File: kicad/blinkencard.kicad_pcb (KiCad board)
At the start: 2 copper layers, 89 x 51 mm, 68 parts, among them Q1 BC847, Q2 BC847, Q3 BC847, Q4 BC847, Q5 BC847, SW1 LEFT, SW2 1, SW3 0, SW4 RIGHT, U1 ICE40UP5K-SG48ITR, U2 ESP32-WROOM-32D

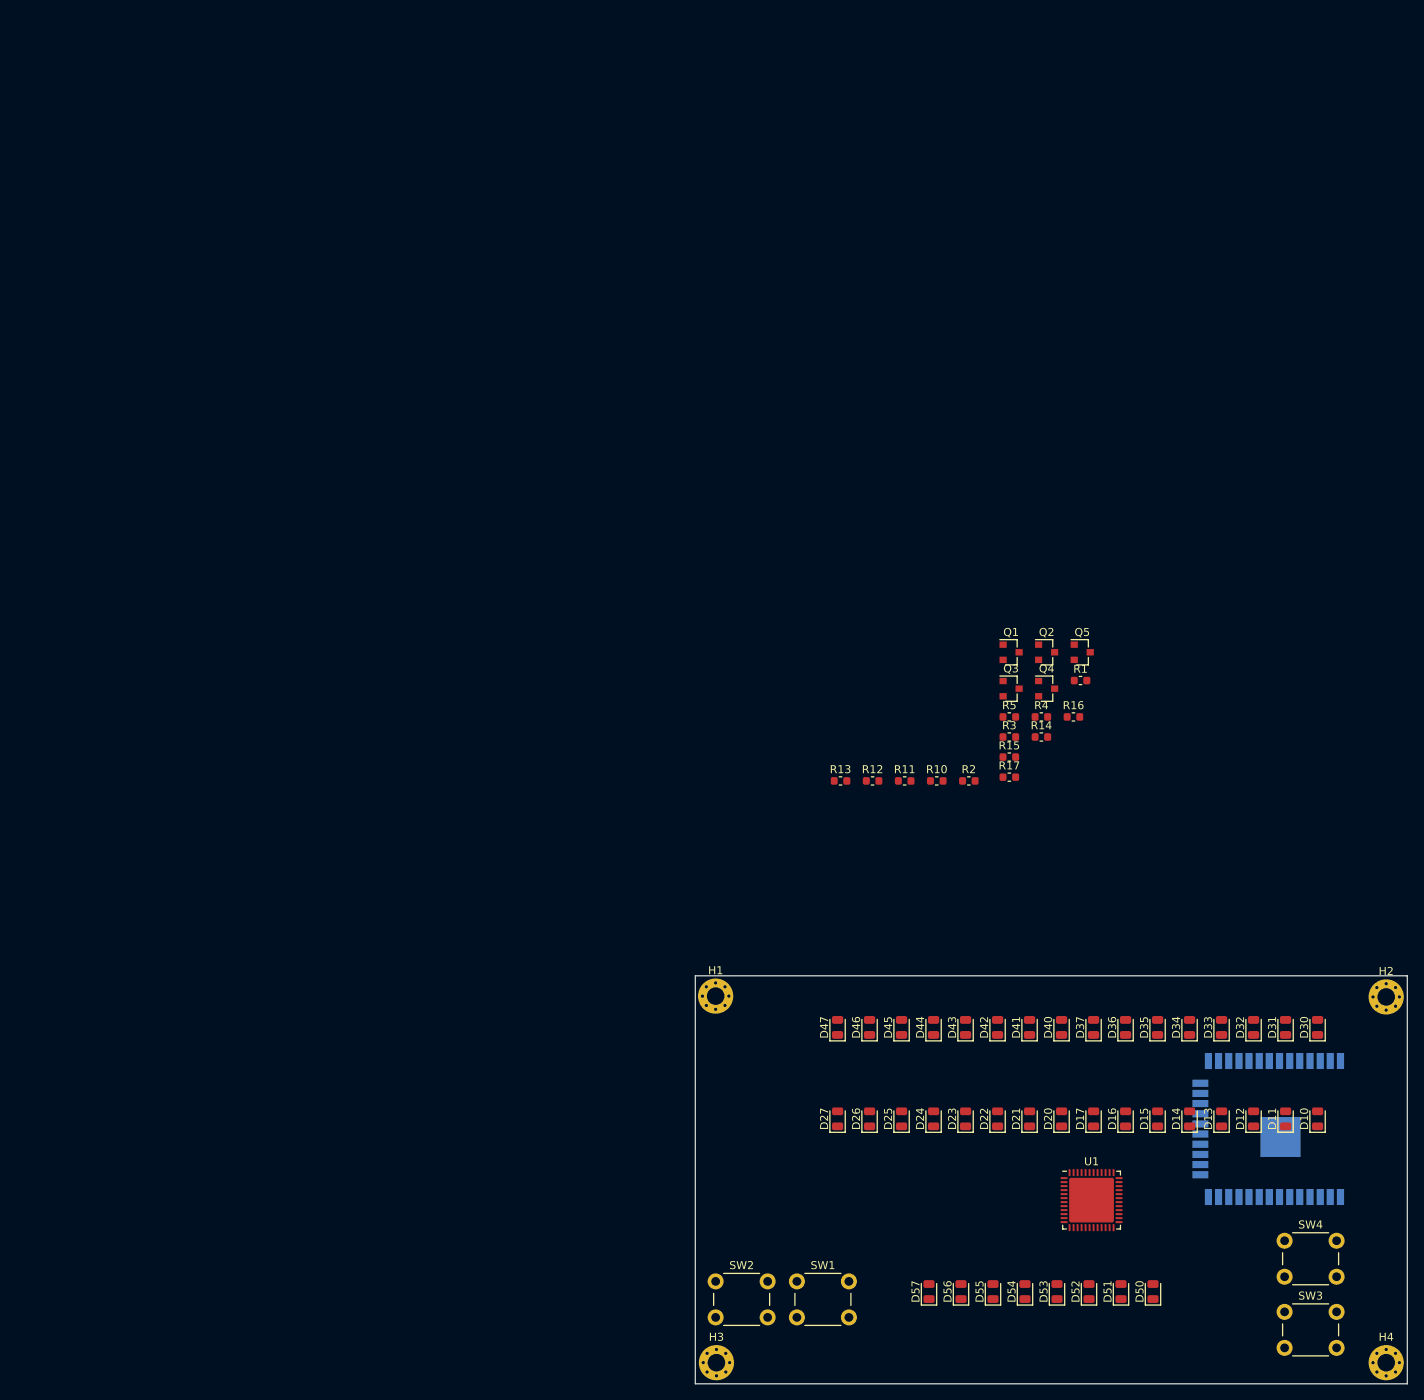
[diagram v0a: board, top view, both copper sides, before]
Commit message: LED layout in progress
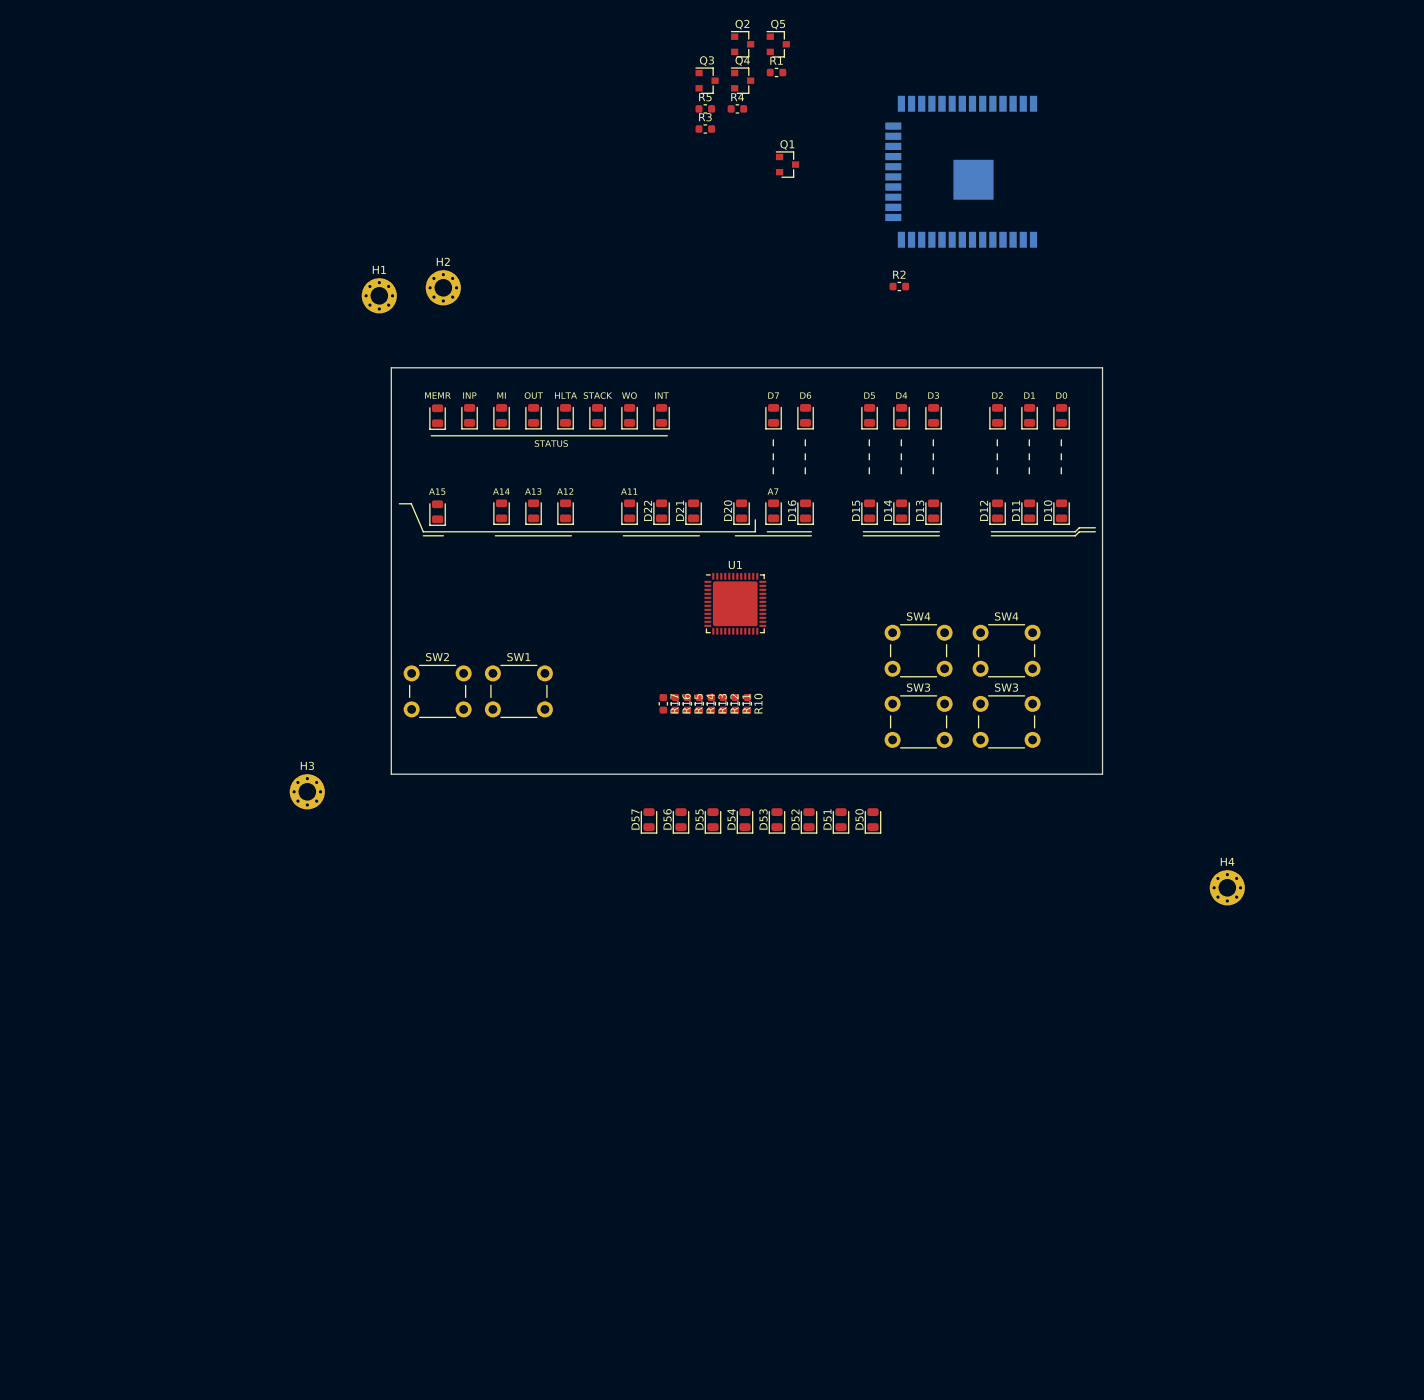
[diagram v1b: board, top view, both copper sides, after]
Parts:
- added SW3: 0, Button_Switch_THT:SW_PUSH_6mm_H5mm, F.Cu at (62.7, 42.0)
- added SW4: RIGHT, Button_Switch_THT:SW_PUSH_6mm_H5mm, F.Cu at (62.7, 33.1)
- moved H2 147.5 mm to (6.50, -10.0)
- moved U2 125.7 mm to (72.0, -24.5)
- moved H1 97.1 mm to (-1.50, -9.00)
- moved D40 91.4 mm to (33.8, 5.95)
- moved D41 91.4 mm to (29.8, 5.95)
- moved D42 91.4 mm to (25.8, 5.95)
- moved D43 91.4 mm to (21.8, 5.95)
- moved D44 91.4 mm to (17.8, 5.95)
- moved D45 91.4 mm to (13.8, 5.95)
- moved D46 91.4 mm to (9.78, 5.95)
- moved D47 91.3 mm to (5.78, 6.00)
- moved D27 90.9 mm to (5.78, 18.0)
- moved D24 88.8 mm to (21.8, 17.9)
- moved D25 88.8 mm to (17.8, 17.9)
- moved D26 88.8 mm to (13.8, 17.9)
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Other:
- board size 89 x 51 mm -> 88.9 x 50.8 mm
- board text added: "STATUS"

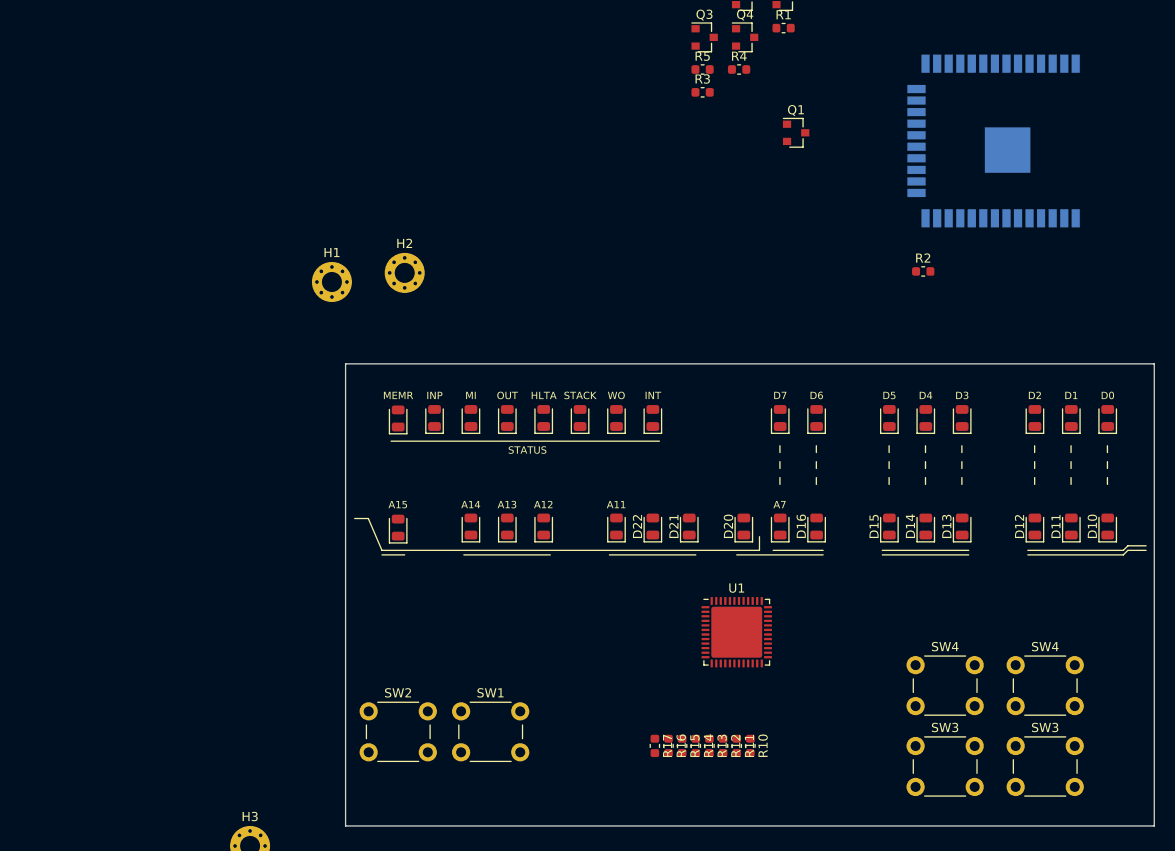
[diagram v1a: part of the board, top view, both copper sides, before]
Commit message: More LED routing
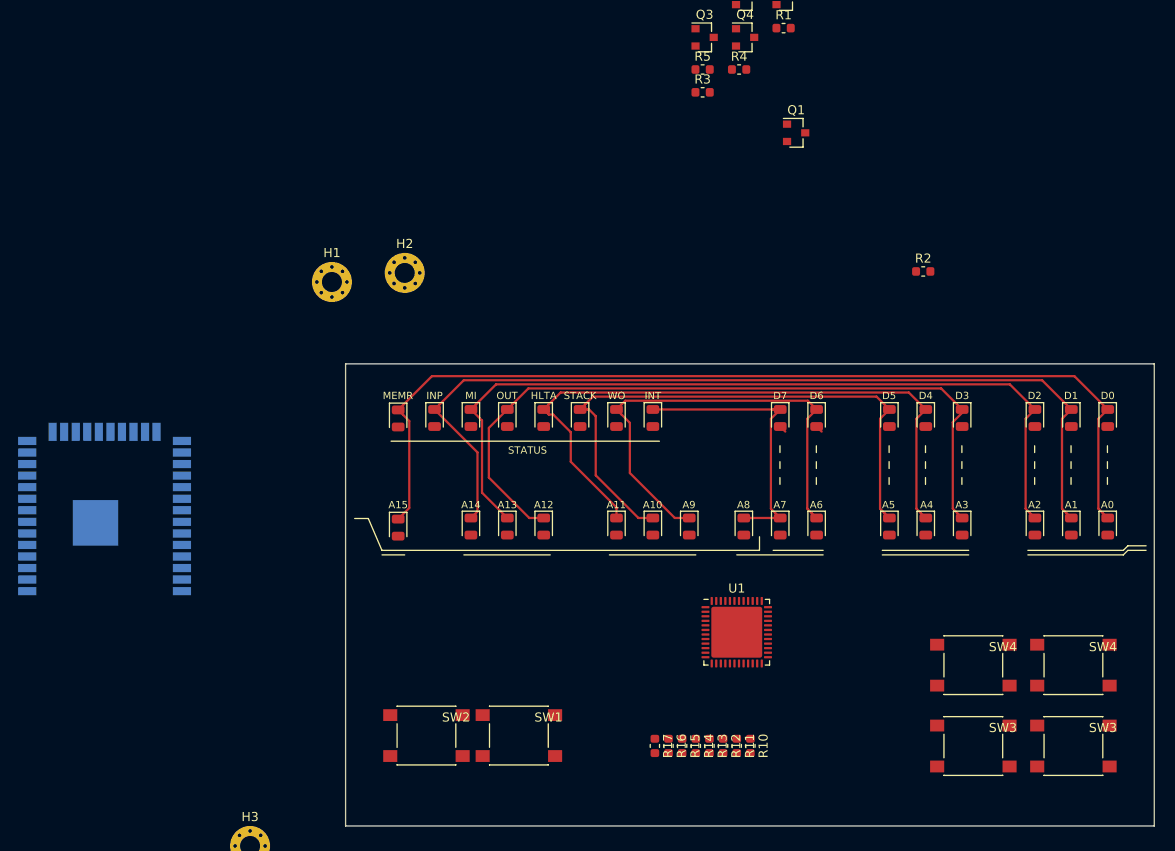
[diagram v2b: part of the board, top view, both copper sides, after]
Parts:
- removed the D12 at (75.8, 17.9)
- added D15: LED_Small, LED_SMD:LED_0805_2012Metric, F.Cu at (75.8, 17.9)
- SW1, SW2, SW3 (x2), SW4 (x2): footprint Button_Switch_THT:SW_PUSH_6mm_H5mm -> Button_Switch_SMD:SW_SPST_PTS645
- moved U2 106.8 mm to (-26.5, 16.7), turned to 0 degrees
- moved SW1 6.88 mm to (19.1, 40.9)
- moved SW2 6.88 mm to (8.89, 40.9)
- moved SW3 6.35 mm to (69.0, 42.0)
- moved SW3 6.35 mm to (80.0, 42.0)
- moved SW4 6.35 mm to (69.0, 33.1)
- moved SW4 6.35 mm to (80.0, 33.1)
- turned D10 to 270 degrees
- turned D11 to 270 degrees
- turned D12 to 270 degrees
- turned D13 to 270 degrees
- turned D14 to 270 degrees
- turned D16 to 270 degrees
- turned D17 to 270 degrees
- turned D20 to 270 degrees
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- renumbered D17 to D10, D16 to D11, D15 to D12, D14 to D13, D13 to D14, D11 to D16, D10 to D17, D37 to D30, D36 to D31, D35 to D32, D34 to D33, D33 to D34, D32 to D35, D31 to D36, D30 to D37
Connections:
- D10 pad 1: Net-(D17-Pad1) -> Net-(D10-Pad1)
- D11 pad 1: Net-(D16-Pad1) -> Net-(D11-Pad1)
- D12 pad 1: Net-(D15-Pad1) -> Net-(D12-Pad1)
- D13 pad 1: Net-(D14-Pad1) -> Net-(D13-Pad1)
- D14 pad 1: Net-(D13-Pad1) -> Net-(D14-Pad1)
- D16 pad 1: Net-(D11-Pad1) -> Net-(D16-Pad1)
- D17 pad 1: Net-(D10-Pad1) -> Net-(D17-Pad1)
- D30 pad 1: Net-(D17-Pad1) -> Net-(D10-Pad1)
- D31 pad 1: Net-(D16-Pad1) -> Net-(D11-Pad1)
- D32 pad 1: Net-(D15-Pad1) -> Net-(D12-Pad1)
- D33 pad 1: Net-(D14-Pad1) -> Net-(D13-Pad1)
- D34 pad 1: Net-(D13-Pad1) -> Net-(D14-Pad1)
- D35 pad 1: Net-(D12-Pad1) -> Net-(D15-Pad1)
- D36 pad 1: Net-(D11-Pad1) -> Net-(D16-Pad1)
- D37 pad 1: Net-(D10-Pad1) -> Net-(D17-Pad1)
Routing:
- net Net-(D17-Pad1): track 0.00 -> 106.8 mm
- net Net-(D16-Pad1): track 0.00 -> 99.6 mm
- net Net-(D15-Pad1): track 0.00 -> 90.7 mm
- net Net-(D14-Pad1): track 0.00 -> 80.9 mm
- net Net-(D13-Pad1): track 0.00 -> 71.8 mm
- net Net-(D12-Pad1): track 0.00 -> 64.7 mm
- net Net-(D11-Pad1): track 0.00 -> 51.8 mm
- net Net-(D10-Pad1): track 0.00 -> 30.8 mm
- net Net-(D30-Pad2): track 0.00 -> 1.57 mm
